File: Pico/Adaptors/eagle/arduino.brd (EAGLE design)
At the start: 57.1 x 53.3 mm, 6 parts, among them J1 JST-2P-SMD-PW-3410050P1

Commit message: minor board tweaks
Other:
- board text added: "Pico This Side"
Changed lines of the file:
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@@
 rev 1.0</text>
 <text x="49.53" y="13.97" size="1.4224" layer="25" rot="R90">espruino.com/ArduinoPico</text>
+<text x="3.81" y="22.225" size="1.016" layer="25">Pico This Side</text>
 </plain>
 <attributes>
@@
 <element name="U$1" library="espruino_pico" package="ESPRUINO_PICO_SMD" value="ESPRUINO_PICO_SMD" x="15.367" y="22.86"/>
 <element name="R1" library="rcl" package="R0805" value="10k" x="8.89" y="43.18" smashed="yes" rot="R270">
-<attribute name="NAME" x="8.255" y="40.64" size="1.27" layer="25" rot="R270"/>
+<attribute name="NAME" x="5.588" y="41.783" size="1.27" layer="25"/>
 </element>
 <element name="R2" library="rcl" package="R0805" value="10k" x="11.43" y="43.18" smashed="yes" rot="R270">
-<attribute name="NAME" x="10.795" y="40.64" size="1.27" layer="25" rot="R270"/>
+<attribute name="NAME" x="13.335" y="41.91" size="1.27" layer="25"/>
 </element>
 <element name="J1" library="OPL Eagle Library" package="2P-SMD-2.0-90D" value="JST-2P-SMD-PW-3410050P1" x="3.81" y="37.465" smashed="yes" rot="R270"/>

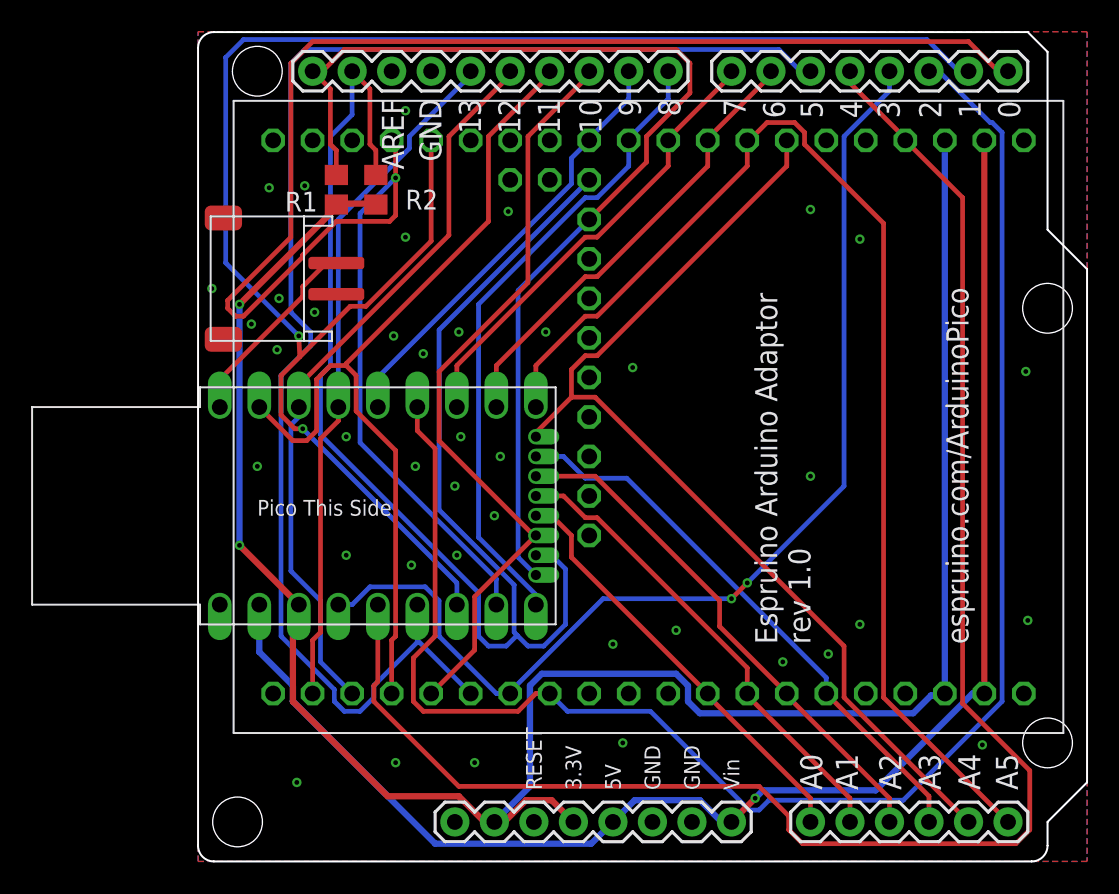
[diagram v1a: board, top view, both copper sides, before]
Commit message: added battery charger IC
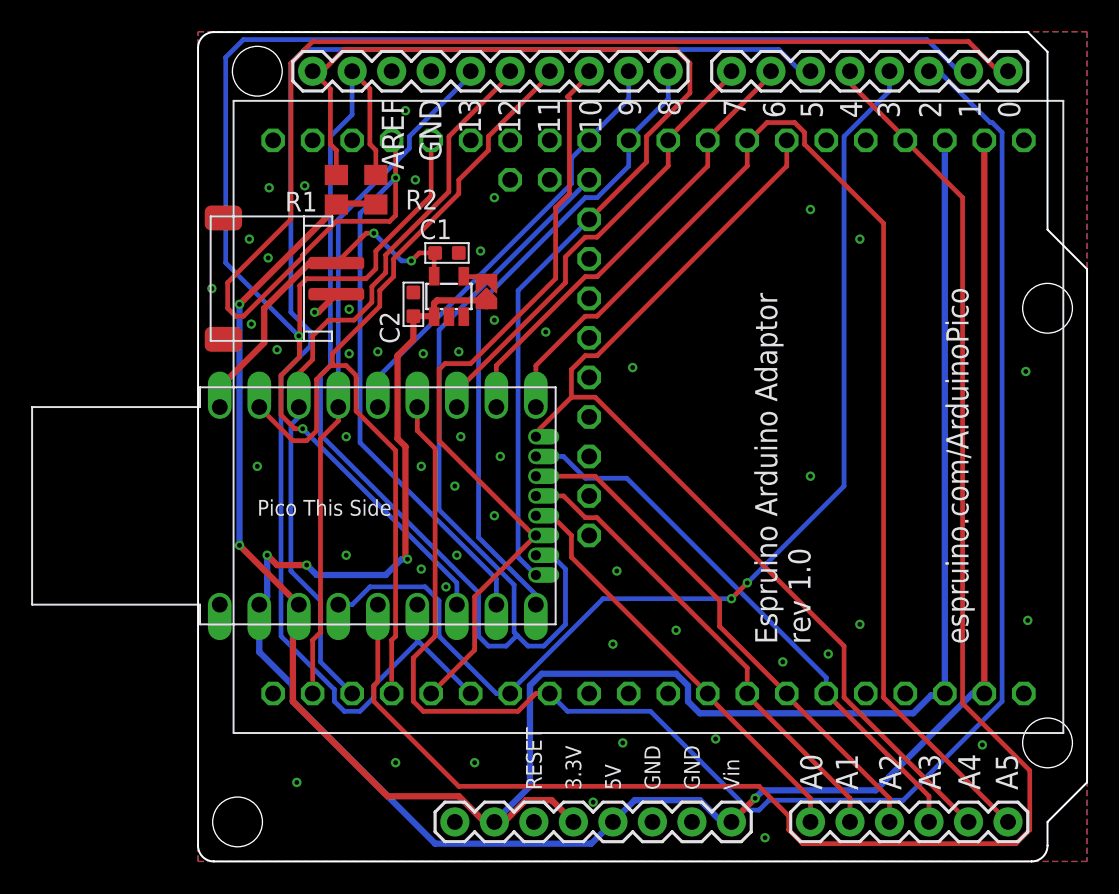
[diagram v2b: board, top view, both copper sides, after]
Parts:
- added C1, C2: 100nF, OPL5:C0603
- added U$4: SOLDERJUMPER, solder_jumper:SOLDERJUMPER
- added U3: MAX1551, template:SOT23-5
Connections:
- removed net N$1: J1.+, U$1.BAT
- new net BAT: C1.1, J1.+, U$1.BAT, U3.5
- new net N$2: U$4.P$1, U3.4
- net GND: now also C1.2, C2.2, U3.2
- net VIN: now also C2.1, U$4.P$2, U3.1
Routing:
- net VIN: track 96.1 -> 131.5 mm, vias 1 -> 4
- net BAT: track 0.00 -> 23.0 mm, vias 0 -> 2
- net N$1: track 12.8 -> 0.00 mm
- net GND: track 0.00 -> 1.88 mm, vias 40 -> 50
- net D1: track 109.7 -> 111.3 mm
- net N$2: track 0.00 -> 1.48 mm
- net D10: track 49.4 -> 50.5 mm
- net D12: track 47.5 -> 48.4 mm

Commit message: Added battery charger pads to proto headers
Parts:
- J1: value JST-2P-SMD-PW-3410050P1 -> (none)
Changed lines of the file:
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@@
 <attribute name="NAME" x="13.335" y="41.91" size="1.27" layer="25"/>
 </element>
-<element name="J1" library="OPL Eagle Library" package="2P-SMD-2.0-90D" value="JST-2P-SMD-PW-3410050P1" x="3.81" y="37.465" smashed="yes" rot="R270"/>
+<element name="J1" library="OPL Eagle Library" package="2P-SMD-2.0-90D" value="" x="3.81" y="37.465" smashed="yes" rot="R270"/>
 <element name="U3" library="template" package="SOT23-5" value="MAX1551" x="16.129" y="36.322" smashed="yes">
 <attribute name="VALUE" x="15.3035" y="33.4645" size="0.635" layer="27" ratio="10"/>
